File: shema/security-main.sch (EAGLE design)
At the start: 41 parts, among them Q1 70TO3GH, Q2 2N4403, X1 DOOR-SENSORS

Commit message: pc2 keyboard
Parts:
- added F2: (no value), fuse:TE5
- added X2: PC/2 Keyboard, con-yamaichi:MD06SS
- D5, D6: value MBRA340T3 -> (none); device diode:MBRA340T3 -> zetex:DS_E2L
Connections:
- new net KBD_CLOCK: X2.5
- new net KBD_DATA: X2.1
- new net N$14: F2.2, JP6.1
- net GND: now also X2.3
- net N$9: now also D6.K, F2.1; no longer D6.C, JP6.1
- net V+: now also D5.K, X2.4; no longer D5.C
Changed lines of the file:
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@@
 <part name="C5" library="capacitor-wima" deviceset="C" device="2,5-3" value="0.1"/>
 <part name="JP3" library="pinhead" deviceset="PINHD-1X5" device="" value="PICkit2"/>
-<part name="D5" library="diode" deviceset="MBRA340T3" device="" value=""/>
+<part name="D5" library="zetex" deviceset="DS_E2L" device=""/>
 <part name="R5" library="resistor" deviceset="R-EU_" device="0204/2V" value="10k"/>
 <part name="SUPPLY7" library="supply2" deviceset="V+" device=""/>
@@
 <part name="U$2" library="lex-library" deviceset="MP1405" device=""/>
 <part name="G1" library="battery" deviceset="CRAA" device="" value="18650"/>
-<part name="D6" library="diode" deviceset="MBRA340T3" device="" value=""/>
+<part name="D6" library="zetex" deviceset="DS_E2L" device=""/>
 <part name="JP6" library="pinhead" deviceset="PINHD-1X2" device="/90" value="POWER"/>
 <part name="F1" library="fuse" deviceset="TE5" device=""/>
 <part name="SUPPLY1" library="supply2" deviceset="V+" device="" value="~"/>
 <part name="SUPPLY2" library="supply2" deviceset="V+" device="" value="~"/>
+<part name="F2" library="fuse" deviceset="TE5" device=""/>
+<part name="X2" library="con-yamaichi" deviceset="MD06SS" device="" value="PC/2 Keyboard"/>
 </parts>
 <sheets>
@@
 <instance part="C5" gate="G$1" x="147.32" y="106.68"/>
 <instance part="JP3" gate="A" x="5.08" y="116.84" rot="R90"/>
-<instance part="D5" gate="G$1" x="160.02" y="106.68" rot="R180"/>
+<instance part="D5" gate="A" x="165.1" y="106.68" rot="R180"/>
 <instance part="R5" gate="G$1" x="83.82" y="20.32" rot="R90"/>
 <instance part="SUPPLY7" gate="1" x="83.82" y="30.48"/>
@@
 <attribute name="VALUE" x="142.24" y="147.32" size="1.778" layer="96" rot="R180"/>
 </instance>
-<instance part="D6" gate="G$1" x="149.86" y="149.86"/>
+<instance part="D6" gate="A" x="139.7" y="149.86"/>
 <instance part="JP6" gate="G$1" x="177.8" y="147.32"/>
 <instance part="F1" gate="1" x="10.16" y="149.86"/>
 <instance part="SUPPLY1" gate="1" x="-10.16" y="149.86" rot="R90"/>
 <instance part="SUPPLY2" gate="1" x="-10.16" y="132.08" rot="R90"/>
+<instance part="F2" gate="1" x="162.56" y="149.86"/>
+<instance part="X2" gate="G$1" x="-25.4" y="111.76" rot="R90"/>
 </instances>
 <busses>
@@
 <pinref part="GND16" gate="1" pin="GND"/>
 </segment>
+<segment>
+<pinref part="X2" gate="G$1" pin="3"/>
+<wire x1="-27.94" y1="101.6" x2="-27.94" y2="83.82" width="0.1524" layer="91"/>
+<label x="-27.94" y="86.36" size="1.778" layer="95" rot="R90"/>
+</segment>
 </net>
 <net name="V+" class="0">
@@
 <wire x1="147.32" y1="109.22" x2="154.94" y2="109.22" width="0.1524" layer="91"/>
 <junction x="154.94" y="109.22"/>
-<pinref part="D5" gate="G$1" pin="C"/>
-<wire x1="157.48" y1="106.68" x2="154.94" y2="106.68" width="0.1524" layer="91"/>
+<pinref part="D5" gate="A" pin="K"/>
+<wire x1="162.56" y1="106.68" x2="154.94" y2="106.68" width="0.1524" layer="91"/>
 </segment>
 <segment>
@@
 <wire x1="68.58" y1="25.4" x2="68.58" y2="27.94" width="0.1524" layer="91"/>
 </segment>
+<segment>
+<pinref part="X2" gate="G$1" pin="4"/>
+<wire x1="-25.4" y1="101.6" x2="-25.4" y2="83.82" width="0.1524" layer="91"/>
+<label x="-25.4" y="86.36" size="1.778" layer="95" rot="R90"/>
+</segment>
 </net>
 <net name="DOOR" class="0">
@@
 <segment>
 <pinref part="JP1" gate="G$1" pin="1"/>
-<pinref part="D5" gate="G$1" pin="A"/>
-<wire x1="175.26" y1="106.68" x2="162.56" y2="106.68" width="0.1524" layer="91"/>
+<pinref part="D5" gate="A" pin="A"/>
+<wire x1="175.26" y1="106.68" x2="167.64" y2="106.68" width="0.1524" layer="91"/>
 </segment>
 </net>
@@
 <wire x1="68.58" y1="149.86" x2="68.58" y2="157.48" width="0.1524" layer="91"/>
 <junction x="68.58" y="149.86"/>
-<pinref part="D6" gate="G$1" pin="C"/>
-<wire x1="152.4" y1="149.86" x2="157.48" y2="149.86" width="0.1524" layer="91"/>
-<wire x1="157.48" y1="149.86" x2="175.26" y2="149.86" width="0.1524" layer="91"/>
-<wire x1="68.58" y1="157.48" x2="157.48" y2="157.48" width="0.1524" layer="91"/>
-<wire x1="157.48" y1="157.48" x2="157.48" y2="149.86" width="0.1524" layer="91"/>
-<junction x="157.48" y="149.86"/>
-<pinref part="JP6" gate="G$1" pin="1"/>
+<pinref part="D6" gate="A" pin="K"/>
+<wire x1="142.24" y1="149.86" x2="149.86" y2="149.86" width="0.1524" layer="91"/>
+<wire x1="68.58" y1="157.48" x2="149.86" y2="157.48" width="0.1524" layer="91"/>
+<wire x1="149.86" y1="157.48" x2="149.86" y2="149.86" width="0.1524" layer="91"/>
+<pinref part="F2" gate="1" pin="1"/>
+<wire x1="157.48" y1="149.86" x2="149.86" y2="149.86" width="0.1524" layer="91"/>
+<junction x="149.86" y="149.86"/>
 </segment>
 </net>
@@
 <segment>
 <pinref part="U$2" gate="G$1" pin="OUT+"/>
-<wire x1="119.38" y1="149.86" x2="147.32" y2="149.86" width="0.1524" layer="91"/>
-<pinref part="D6" gate="G$1" pin="A"/>
+<wire x1="119.38" y1="149.86" x2="137.16" y2="149.86" width="0.1524" layer="91"/>
+<pinref part="D6" gate="A" pin="A"/>
 </segment>
 </net>
@@
 </segment>
 </net>
+<net name="N$14" class="0">
+<segment>
+<pinref part="F2" gate="1" pin="2"/>
+<pinref part="JP6" gate="G$1" pin="1"/>
+<wire x1="167.64" y1="149.86" x2="175.26" y2="149.86" width="0.1524" layer="91"/>
+</segment>
+</net>
+<net name="KBD_DATA" class="0">
+<segment>
+<pinref part="X2" gate="G$1" pin="1"/>
+<wire x1="-33.02" y1="101.6" x2="-33.02" y2="83.82" width="0.1524" layer="91"/>
+<label x="-33.02" y="86.36" size="1.778" layer="95" rot="R90"/>
+</segment>
+<segment>
+<wire x1="-27.94" y1="78.74" x2="-40.64" y2="78.74" width="0.1524" layer="91"/>
+<label x="-40.64" y="78.74" size="1.778" layer="95"/>
+</segment>
+</net>
+<net name="KBD_CLOCK" class="0">
+<segment>
+<pinref part="X2" gate="G$1" pin="5"/>
+<wire x1="-22.86" y1="101.6" x2="-22.86" y2="83.82" width="0.1524" layer="91"/>
+<label x="-22.86" y="86.36" size="1.778" layer="95" rot="R90"/>
+</segment>
+<segment>
+<wire x1="-12.7" y1="73.66" x2="-40.64" y2="73.66" width="0.1524" layer="91"/>
+<label x="-40.64" y="73.66" size="1.778" layer="95"/>
+</segment>
+</net>

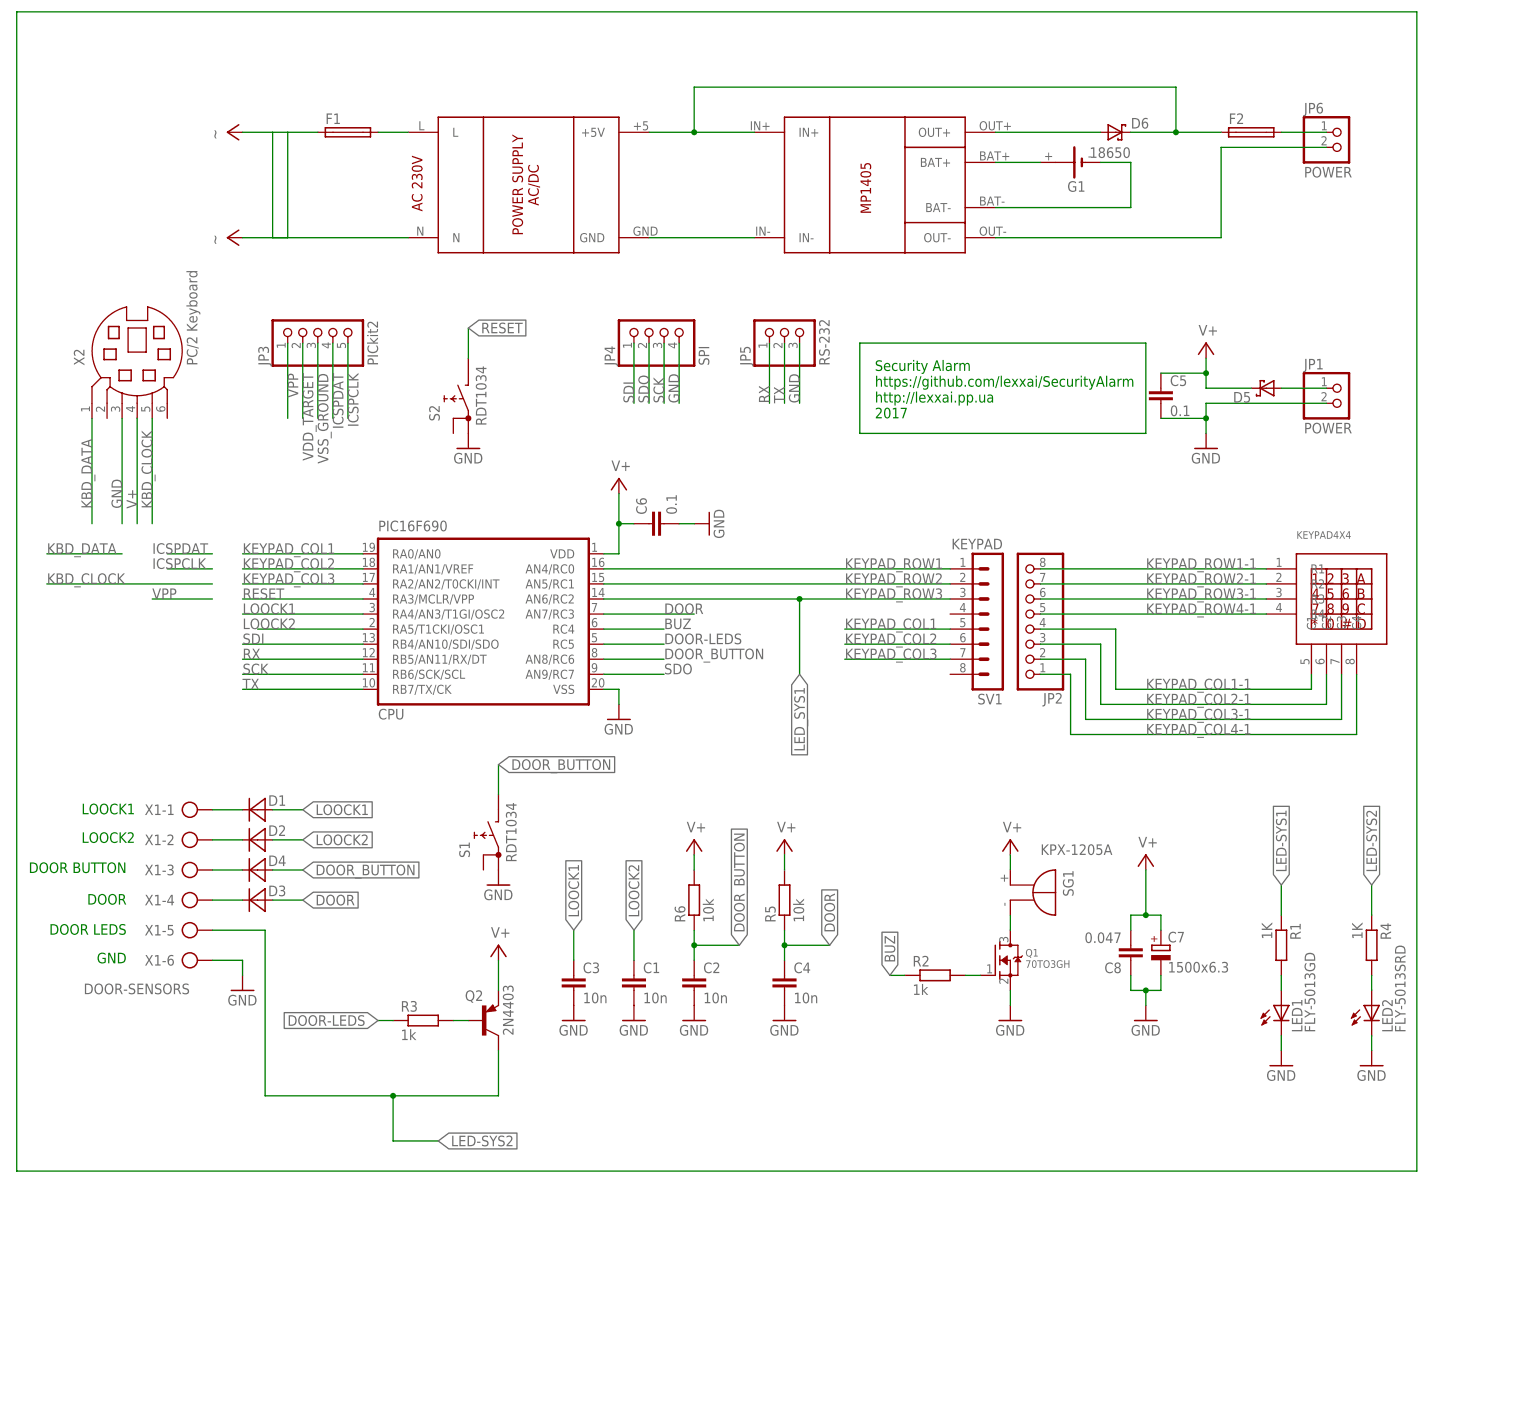
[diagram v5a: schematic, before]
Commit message: Shema changes for iButton protection from High Voltage
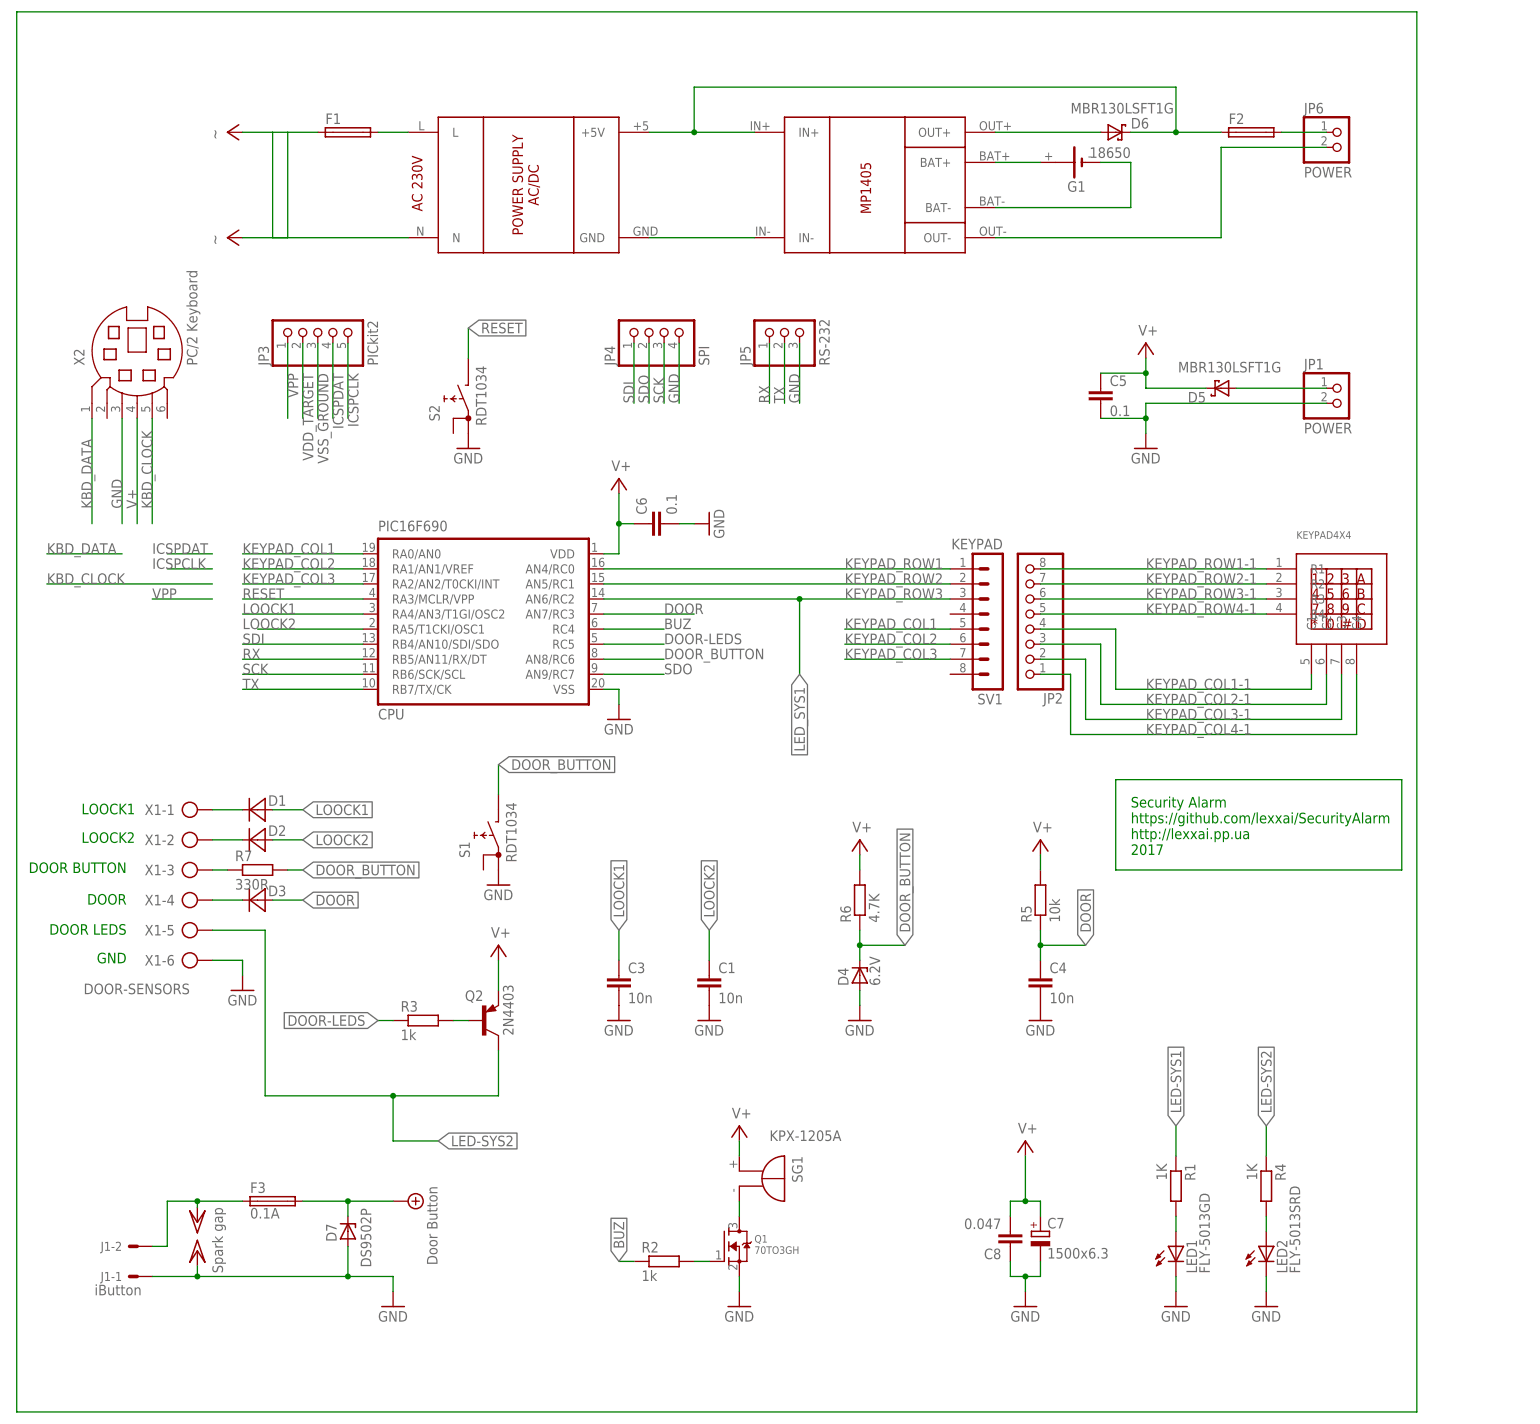
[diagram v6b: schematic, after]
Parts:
- removed C2: 10n, capacitor-wima:C2,5-3
- added D7: DS9502P, diode:ZENER-DIODEZD-12.5
- added F3: 0.1A, fuse:19559
- added J1: iButton, con-molex:22-05-7028-02
- added R7: 330R, resistor:R-EU_0204/2V
- D4: value MBRA340T3 -> 6.2V; device diode:MBRA340T3 -> diode:ZENER-DIODEDO35Z10
- D5, D6: value (none) -> MBR130LSFT1G
- R6: value 10k -> 4.7K
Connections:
- new net +5V: F3.1, J1-2.S
- new net N$21: D7.C, F3.2
- net DOOR_BUTTON: now also D4.C, R7.2; no longer C2.1, D4.A
- net DOOR_BUTTON-1: now also R7.1; no longer D4.C
- net GND: now also D4.A, D7.A, J1-1.S; no longer C2.2
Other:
- moved on the sheet: C1, C3, C4, C5, C7, C8, D5, LED1, LED2, Q1, R1, R2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

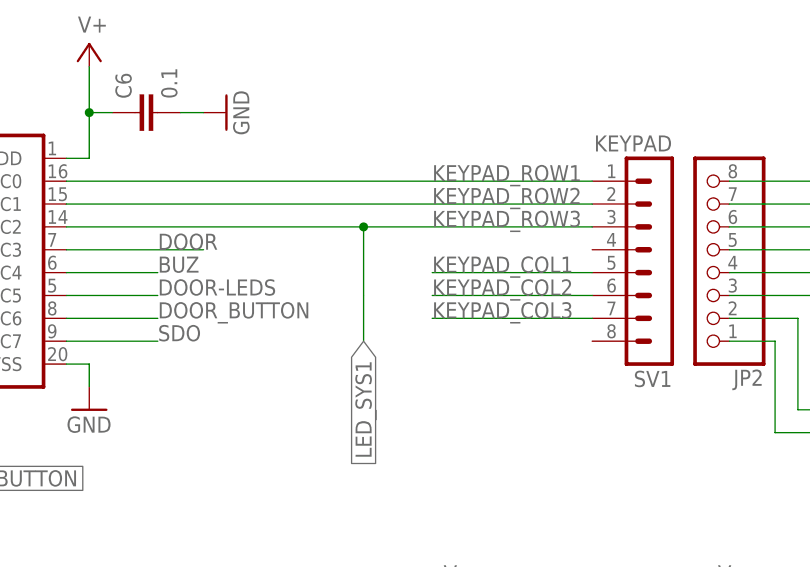
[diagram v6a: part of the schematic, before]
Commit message: key pad 4x3 shema use RC7 for ROW4
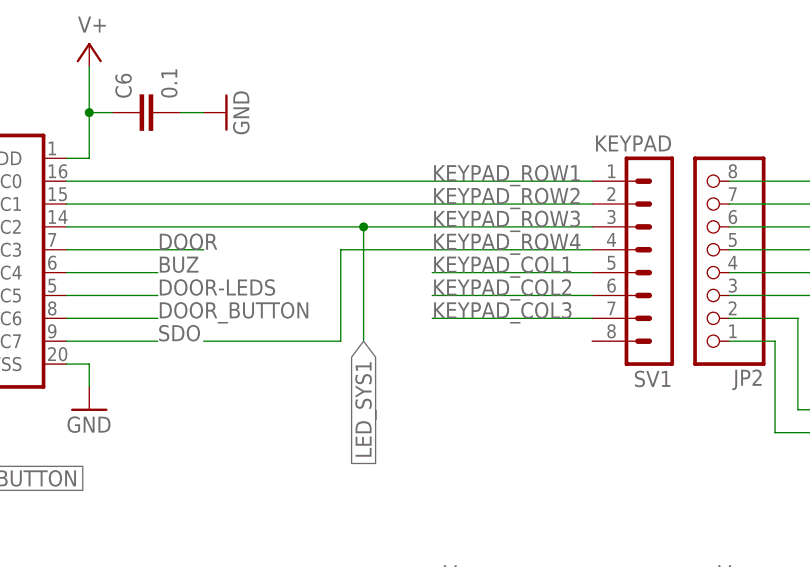
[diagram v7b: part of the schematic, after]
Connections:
- new net KEYPAD_ROW4: SV1.4
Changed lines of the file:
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@@
 <?xml version="1.0" encoding="utf-8"?>
 <!DOCTYPE eagle SYSTEM "eagle.dtd">
-<eagle version="8.2.2">
+<eagle version="9.0.1">
 <drawing>
 <settings>
 <setting alwaysvectorfont="no"/>
+<setting keepoldvectorfont="yes"/>
 <setting verticaltext="up"/>
 </settings>
@@
 </segment>
 </net>
+<net name="KEYPAD_ROW4" class="0">
+<segment>
+<pinref part="SV1" gate="1" pin="4"/>
+<wire x1="111.76" y1="68.58" x2="83.82" y2="68.58" width="0.1524" layer="91"/>
+<label x="93.98" y="68.58" size="1.778" layer="95"/>
+<wire x1="83.82" y1="68.58" x2="83.82" y2="58.42" width="0.1524" layer="91"/>
+<wire x1="83.82" y1="58.42" x2="68.58" y2="58.42" width="0.1524" layer="91"/>
+</segment>
+</net>
